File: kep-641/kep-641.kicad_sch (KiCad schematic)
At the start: 3 parts, among them CN1 Conn_01x06, CN2 To Headphones, CN3 Conn_01x07

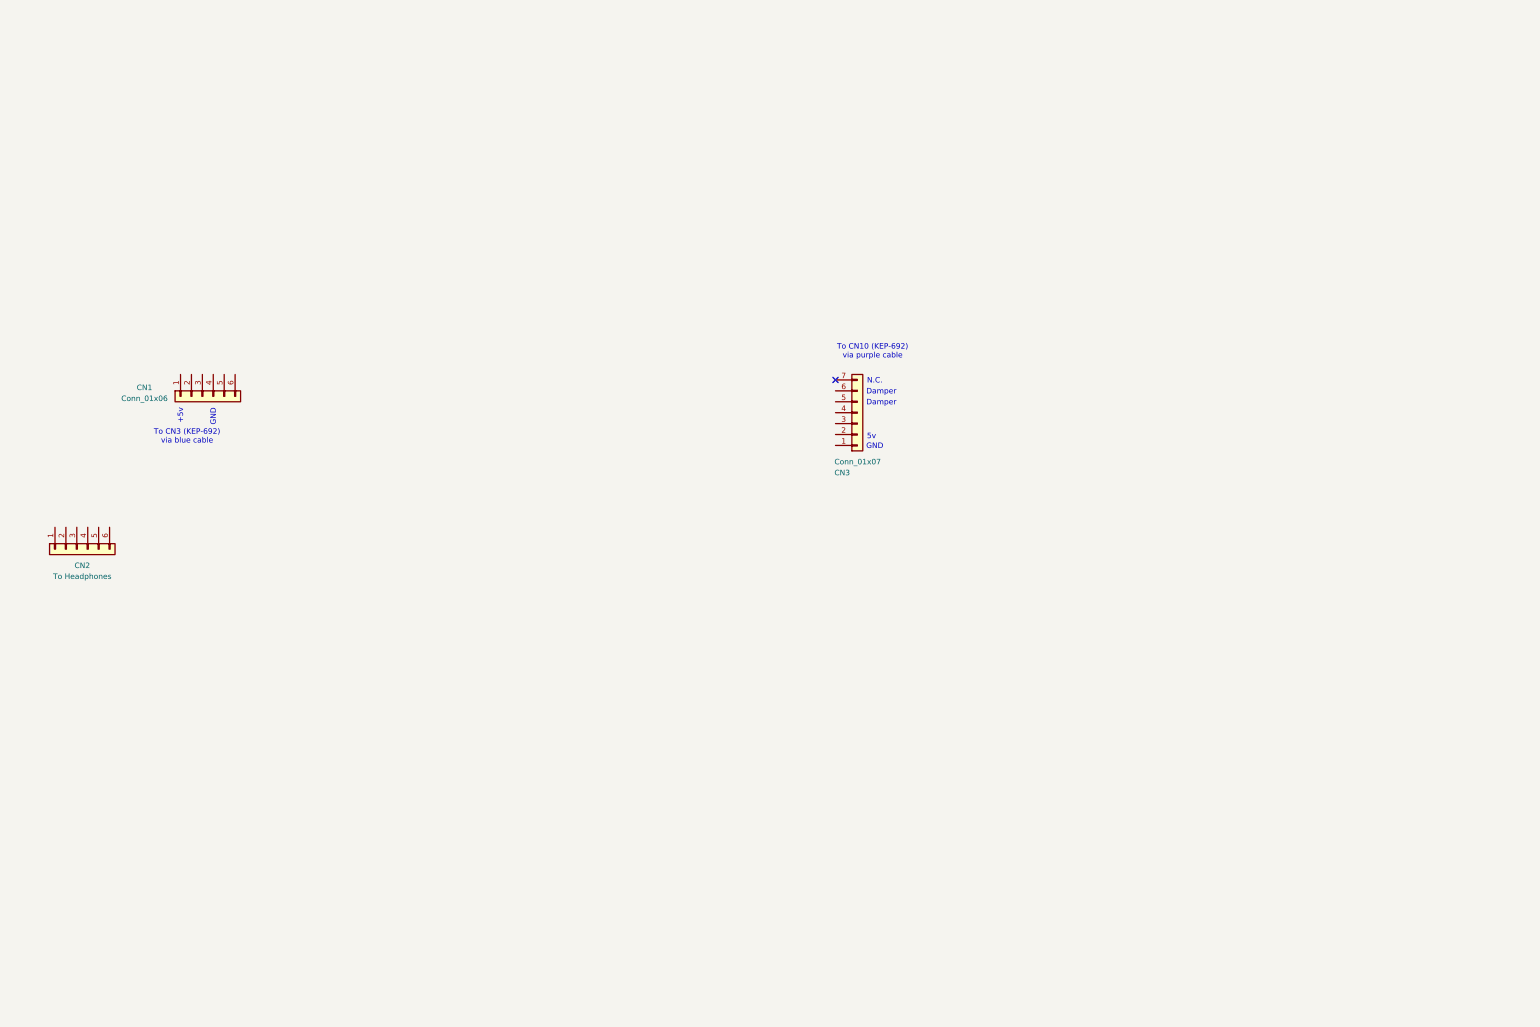
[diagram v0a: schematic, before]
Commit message: Add op-amps. Name the sheet. Resize the page.
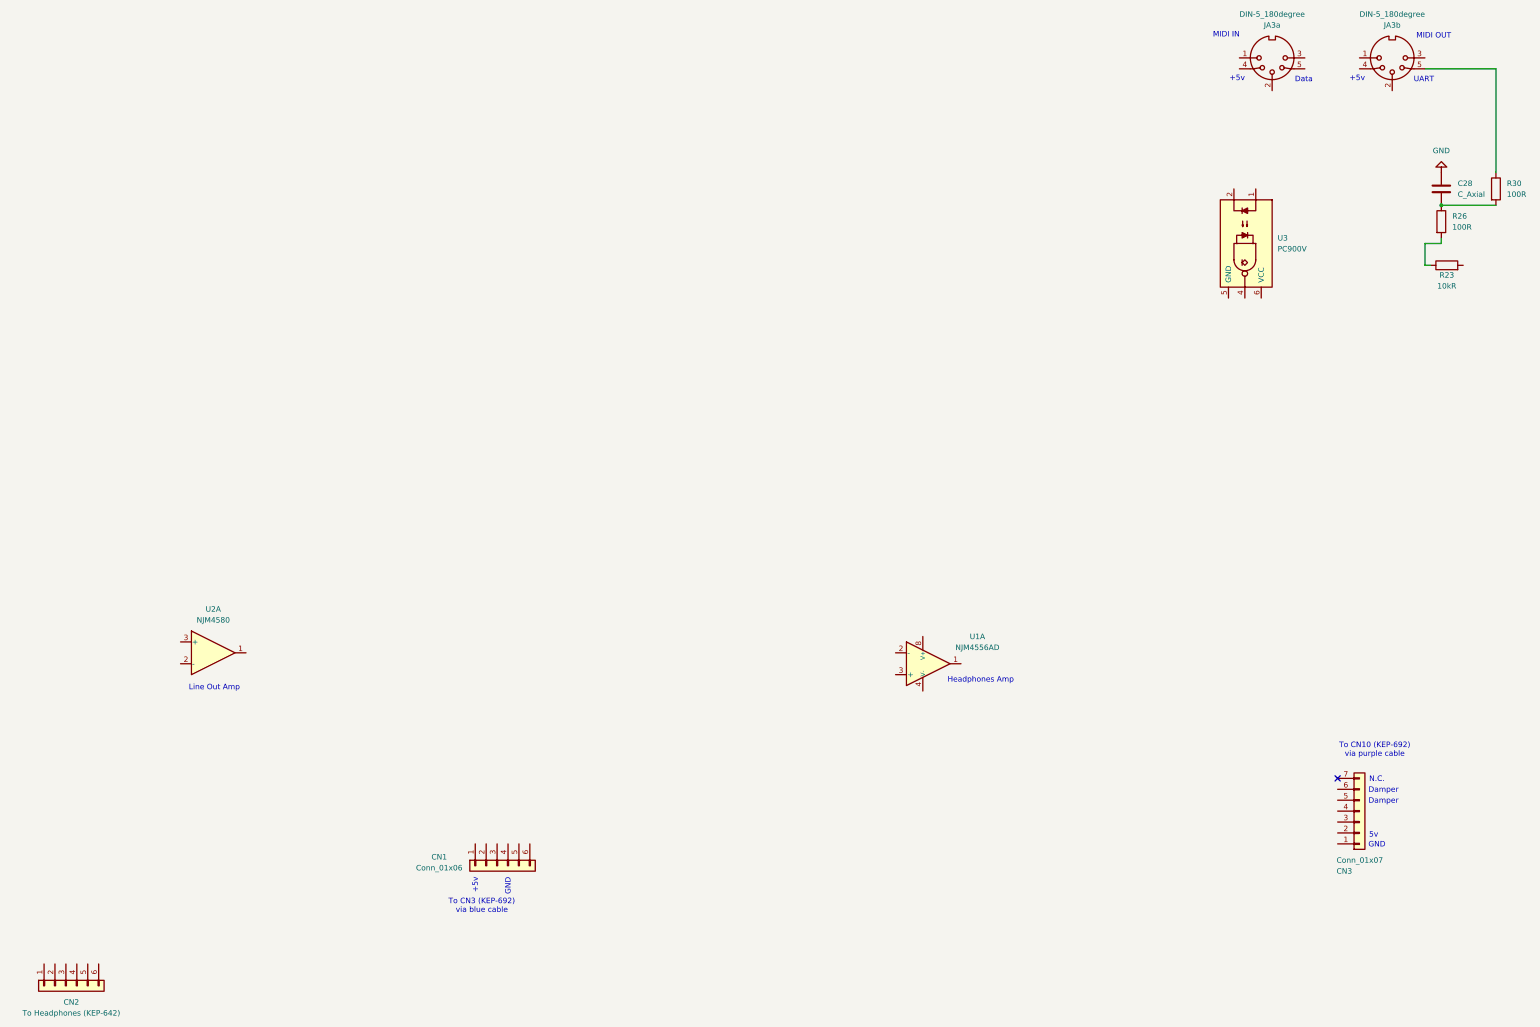
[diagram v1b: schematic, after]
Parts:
- added C28: C_Axial, Capacitor_THT_AKL:C_Axial_L3.0mm_D2.3mm_P5.00mm_Horizontal, symbol PCM_Capacitor_AKL:C_Axial_L3.0mm_D2.3mm_P5.00mm
- added JA3a, JA3b: DIN-5_180degree, symbol Connector:DIN-5_180degree
- added R23: 10kR, symbol Device:R
- added R26, R30: 100R, symbol Device:R
- added U1: NJM4556AD, Package_DIP_AKL:DIP-8_W7.62mm_LongPads, symbol PCM_Amplifier_Operational_AKL:NJM4556AD
- added U2: NJM4580, symbol Amplifier_Operational:NJM4580
- added U3: PC900V, Package_DIP_AKL:DIP-6_W7.62mm_LongPads, symbol PCM_Optocoupler_Logic_AKL:H11L1
- CN2: value To Headphones -> To Headphones (KEP-642)
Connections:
- new net: JA3b.5, R30.1
- new net: C28.2, R26.1, R30.2
- new net: R23.1, R26.2
- new net GND: C28.1
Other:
- note added: "Data"
- note added: "Headphones Amp"
- note added: "Line Out Amp"
- note added: "MIDI IN"
- note added: "MIDI OUT"
- note added: "UART"
- title: (none) -> KEP-641
- moved on the sheet: CN1, CN2, CN3

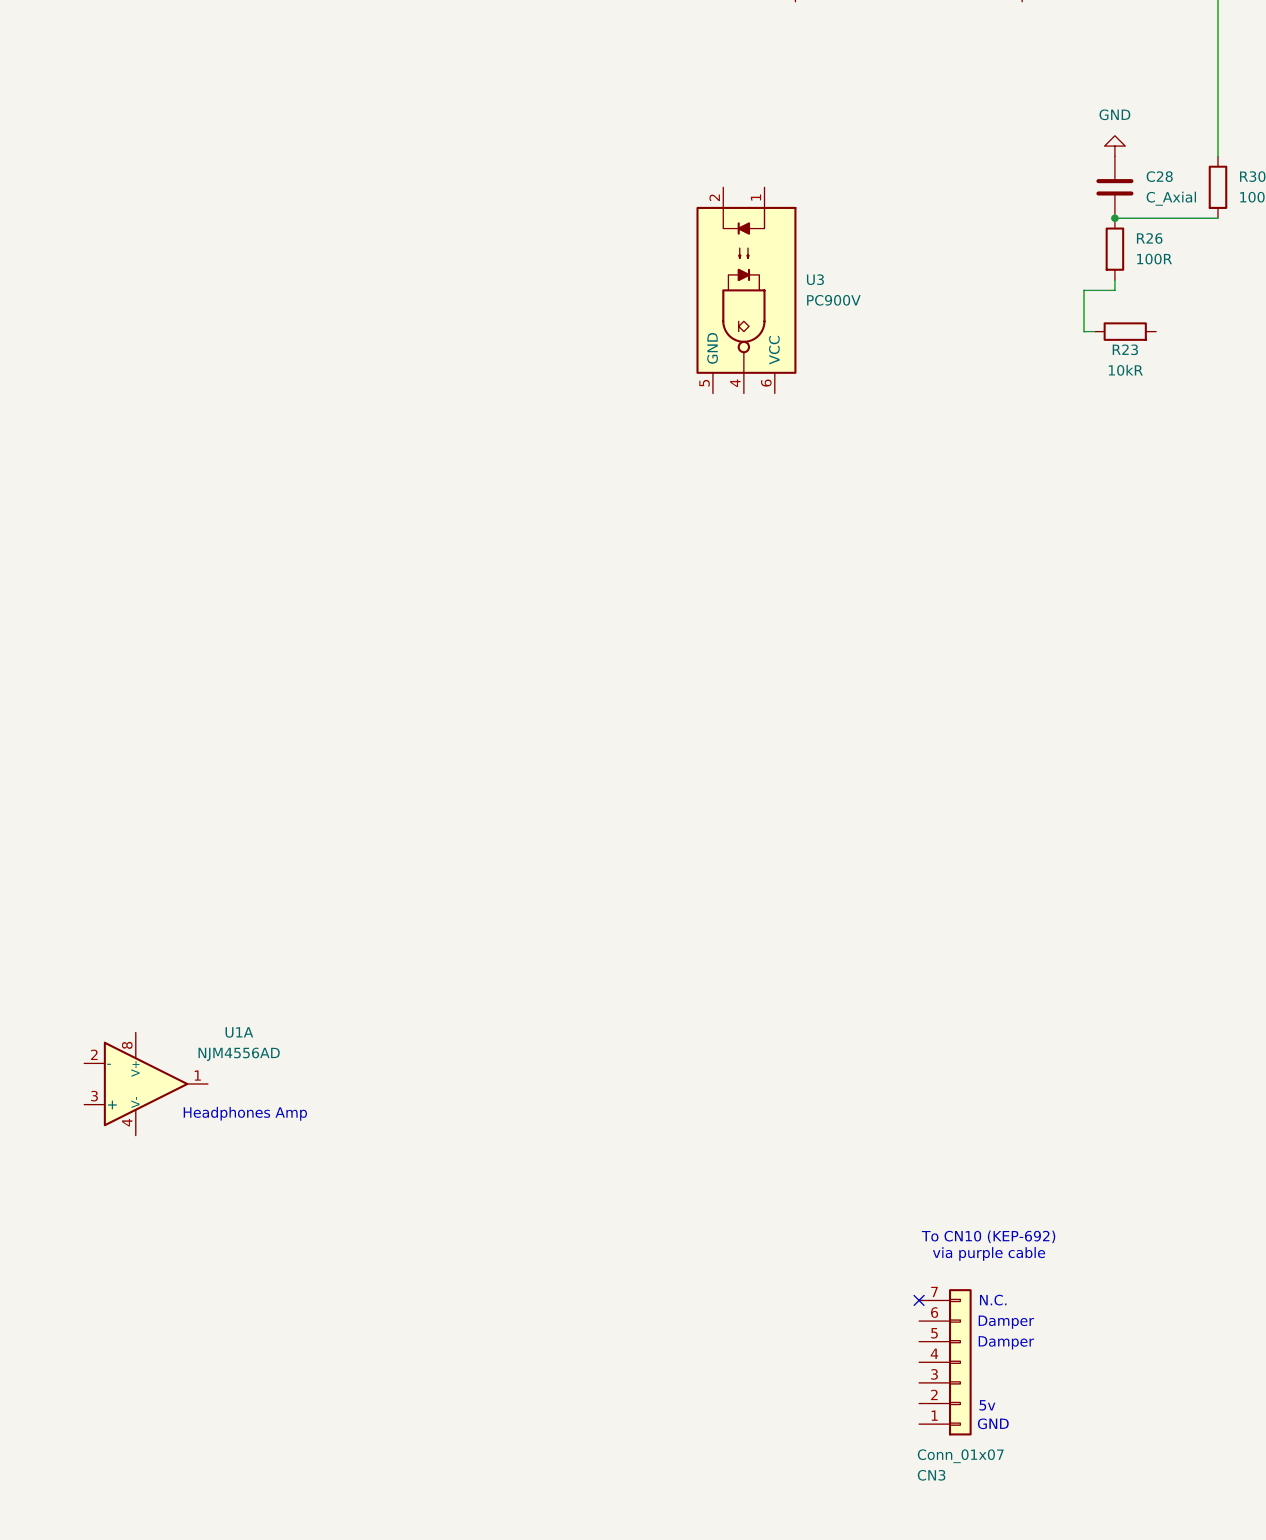
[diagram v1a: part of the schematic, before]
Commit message: Add transistors. Add labels for MIDI signals on CN3. Add ring/sleeve notes on the labels.
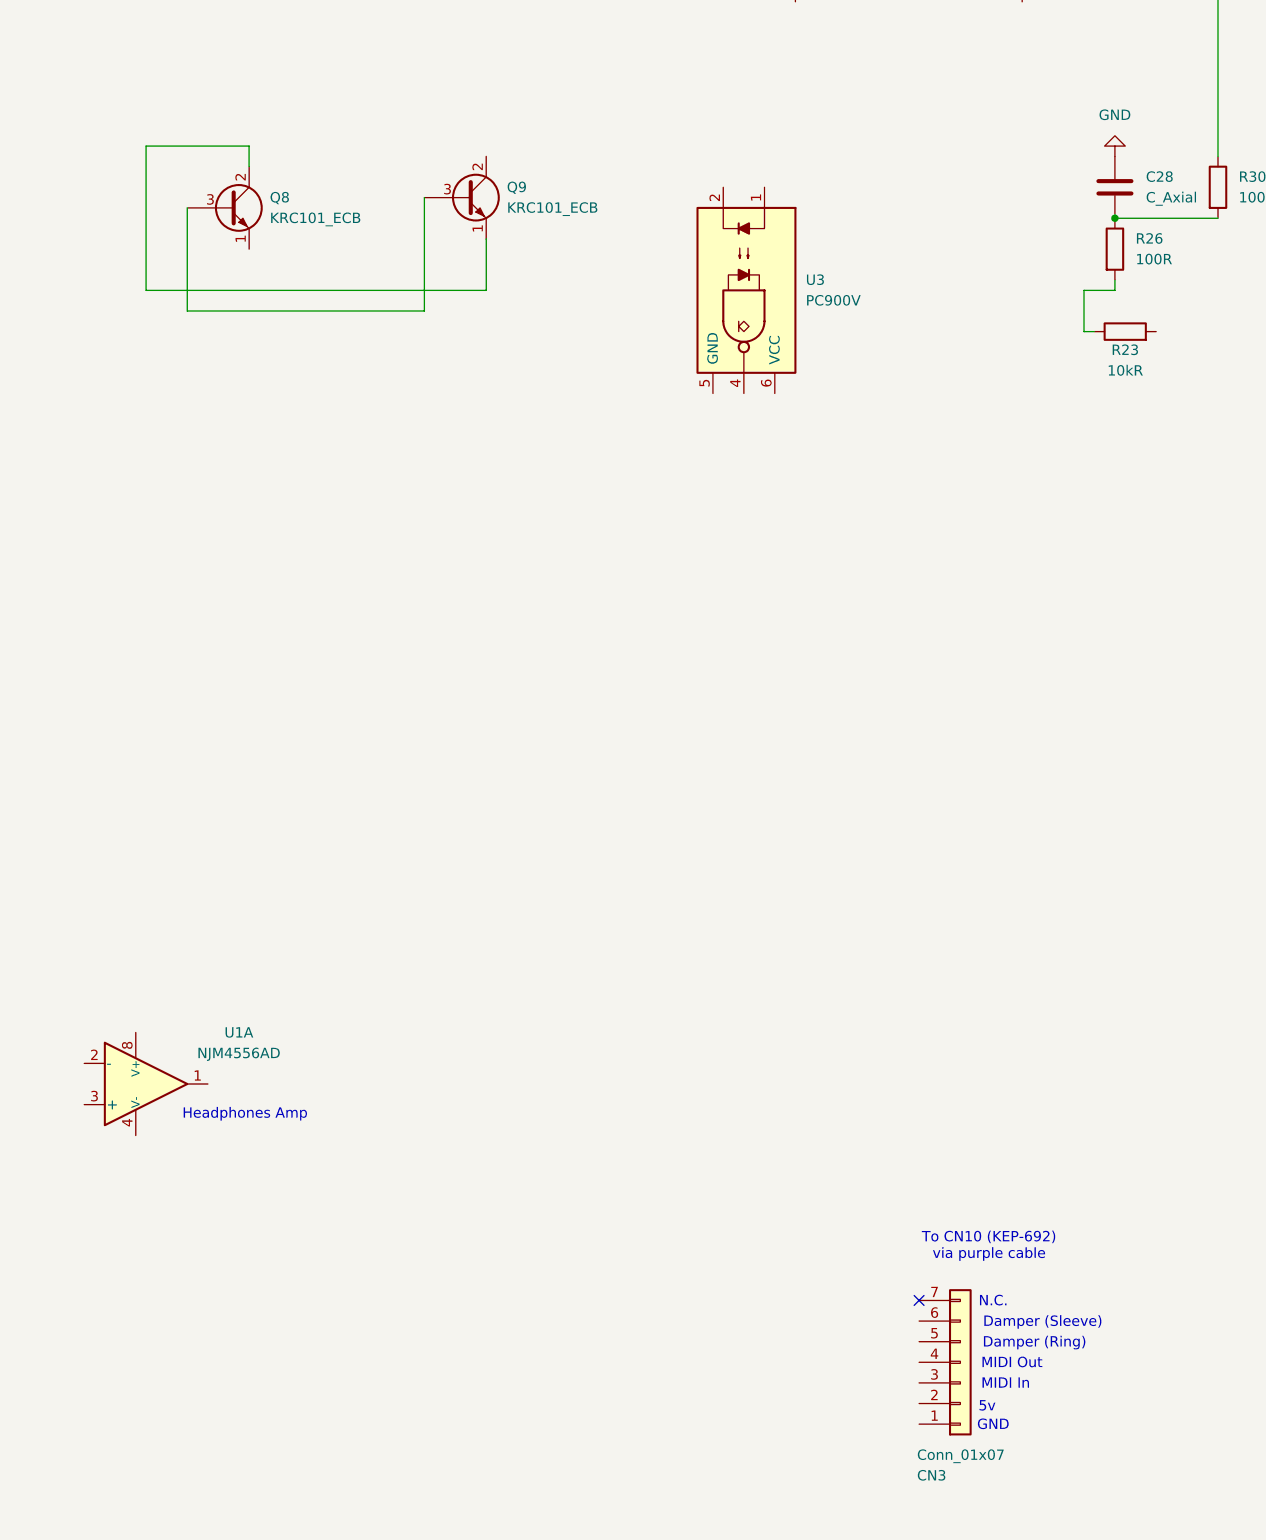
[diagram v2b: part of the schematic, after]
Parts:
- added Q8, Q9: KRC101_ECB, symbol Device:Q_NPN_ECB
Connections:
- new net: Q8.2 (C), Q9.1 (E)
- new net: Q8.3 (B), Q9.3 (B)
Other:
- note added: "Damper (Ring)"
- note added: "Damper (Sleeve)"
- note added: "MIDI In"
- note added: "MIDI Out"
- note removed: "Damper"
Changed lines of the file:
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@@
+	(wire
+		(pts
+			(xy 243.84 55.88) (xy 256.54 55.88)
+		)
+		(stroke
+			(width 0)
+			(type default)
+		)
+	)
 	(wire
 		(pts
@@
 	(wire
 		(pts
+			(xy 248.92 63.5) (xy 248.92 76.2)
+		)
+		(stroke
+			(width 0)
+			(type default)
+		)
+	)
+	(wire
+		(pts
 			(xy 359.41 78.74) (xy 360.68 78.74)
 		)
@@
 	(wire
 		(pts
+			(xy 256.54 55.88) (xy 256.54 58.42)
+		)
+		(stroke
+			(width 0)
+			(type default)
+		)
+	)
+	(wire
+		(pts
 			(xy 363.22 64.77) (xy 375.92 64.77)
 		)
@@
 	(wire
 		(pts
+			(xy 248.92 76.2) (xy 278.13 76.2)
+		)
+		(stroke
+			(width 0)
+			(type default)
+		)
+	)
+	(wire
+		(pts
 			(xy 359.41 33.02) (xy 375.92 33.02)
 		)
@@
 	(wire
 		(pts
+			(xy 243.84 73.66) (xy 243.84 55.88)
+		)
+		(stroke
+			(width 0)
+			(type default)
+		)
+	)
+	(wire
+		(pts
+			(xy 285.75 73.66) (xy 243.84 73.66)
+		)
+		(stroke
+			(width 0)
+			(type default)
+		)
+	)
+	(wire
+		(pts
 			(xy 359.41 73.66) (xy 359.41 78.74)
 		)
@@
 	(wire
 		(pts
+			(xy 285.75 67.31) (xy 285.75 73.66)
+		)
+		(stroke
+			(width 0)
+			(type default)
+		)
+	)
+	(wire
+		(pts
 			(xy 363.22 73.66) (xy 359.41 73.66)
 		)
@@
 		)
 	)
+	(wire
+		(pts
+			(xy 278.13 76.2) (xy 278.13 62.23)
+		)
+		(stroke
+			(width 0)
+			(type default)
+		)
+	)
 	(text "Headphones Amp"
 		(exclude_from_sim no)
@@
 		)
 	)
-	(text "Damper"
-		(exclude_from_sim no)
-		(at 349.758 200.914 0)
+	(text "Damper (Sleeve)"
+		(exclude_from_sim no)
+		(at 354.33 200.914 0)
 		(effects
 			(font
@@
 		)
 	)
+	(text "MIDI Out"
+		(exclude_from_sim no)
+		(at 350.52 205.994 0)
+		(effects
+			(font
+				(size 1.27 1.27)
+			)
+		)
+	)
 	(text "Line Out Amp"
 		(exclude_from_sim no)
@@
 		)
 	)
-	(text "Damper"
-		(exclude_from_sim no)
-		(at 349.758 203.454 0)
+	(text "Damper (Ring)"
+		(exclude_from_sim no)
+		(at 353.314 203.454 0)
 		(effects
 			(font
@@
 		(exclude_from_sim no)
 		(at 343.662 35.306 0)
+		(effects
+			(font
+				(size 1.27 1.27)
+			)
+		)
+	)
+	(text "MIDI In"
+		(exclude_from_sim no)
+		(at 349.758 208.534 0)
 		(effects
 			(font
@@
 					(unit 1)
 				)
+			)
+		)
+	)
+	(symbol
+		(lib_id "Device:Q_NPN_ECB")
+		(at 254 63.5 0)
+		(unit 1)
+		(exclude_from_sim no)
+		(in_bom yes)
+		(on_board yes)
+		(dnp no)
+		(fields_autoplaced yes)
+		(property "Reference" "Q8"
+			(at 259.08 62.2299 0)
+			(effects
+				(font
+					(size 1.27 1.27)
+				)
+				(justify left)
+			)
+		)
+		(property "Value" "KRC101_ECB"
+			(at 259.08 64.7699 0)
+			(effects
+				(font
+					(size 1.27 1.27)
+				)
+				(justify left)
+			)
+		)
+		(property "Footprint" ""
+			(at 259.08 60.96 0)
+			(effects
+				(font
+					(size 1.27 1.27)
+				)
+				(hide yes)
+			)
+		)
+		(property "Datasheet" "~"
+			(at 254 63.5 0)
+			(effects
+				(font
+					(size 1.27 1.27)
+				)
+				(hide yes)
+			)
+		)
+		(property "Description" "NPN transistor, emitter/collector/base"
+			(at 254 63.5 0)
+			(effects
+				(font
+					(size 1.27 1.27)
+				)
+				(hide yes)
+			)
+		)
+		(pin "2"
+		)
+		(pin "1"
+		)
+		(pin "3"
+		)
+		(instances
+			(project ""
+				(path "/8bd6edd5-07c4-40ef-8f26-5a7ff5a2f4c9"
+					(reference "Q8")
+					(unit 1)
+				)
+			)
+		)
+	)
+	(symbol
+		(lib_id "Device:Q_NPN_ECB")
+		(at 283.21 62.23 0)
+		(unit 1)
+		(exclude_from_sim no)
+		(in_bom yes)
+		(on_board yes)
+		(dnp no)
+		(fields_autoplaced yes)
+		(property "Reference" "Q9"
+			(at 288.29 60.9599 0)
+			(effects
+				(font
+					(size 1.27 1.27)
+				)
+				(justify left)
+			)
+		)
+		(property "Value" "KRC101_ECB"
+			(at 288.29 63.4999 0)
+			(effects
+				(font
+					(size 1.27 1.27)
+				)
+				(justify left)
+			)
+		)
+		(property "Footprint" ""
+			(at 288.29 59.69 0)
+			(effects
+				(font
+					(size 1.27 1.27)
+				)
+				(hide yes)
+			)
+		)
+		(property "Datasheet" "~"
+			(at 283.21 62.23 0)
+			(effects
+				(font
+					(size 1.27 1.27)
+				)
+				(hide yes)
+			)
+		)
+		(property "Description" "NPN transistor, emitter/collector/base"
+			(at 283.21 62.23 0)
+			(effects
+				(font
+					(size 1.27 1.27)
+				)
+				(hide yes)
+			)
+		)
+		(pin "2"
+		)
+		(pin "1"
+		)
+		(pin "3"
+		)
+		(instances
+			(project "kep-641"
+				(path "/8bd6edd5-07c4-40ef-8f26-5a7ff5a2f4c9"
+					(reference "Q9")
+					(unit 1)
+				)
